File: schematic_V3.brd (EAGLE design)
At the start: 77.7 x 62.1 mm, 20 parts, among them IC1 VR1, J1 POWER_JACKPTH

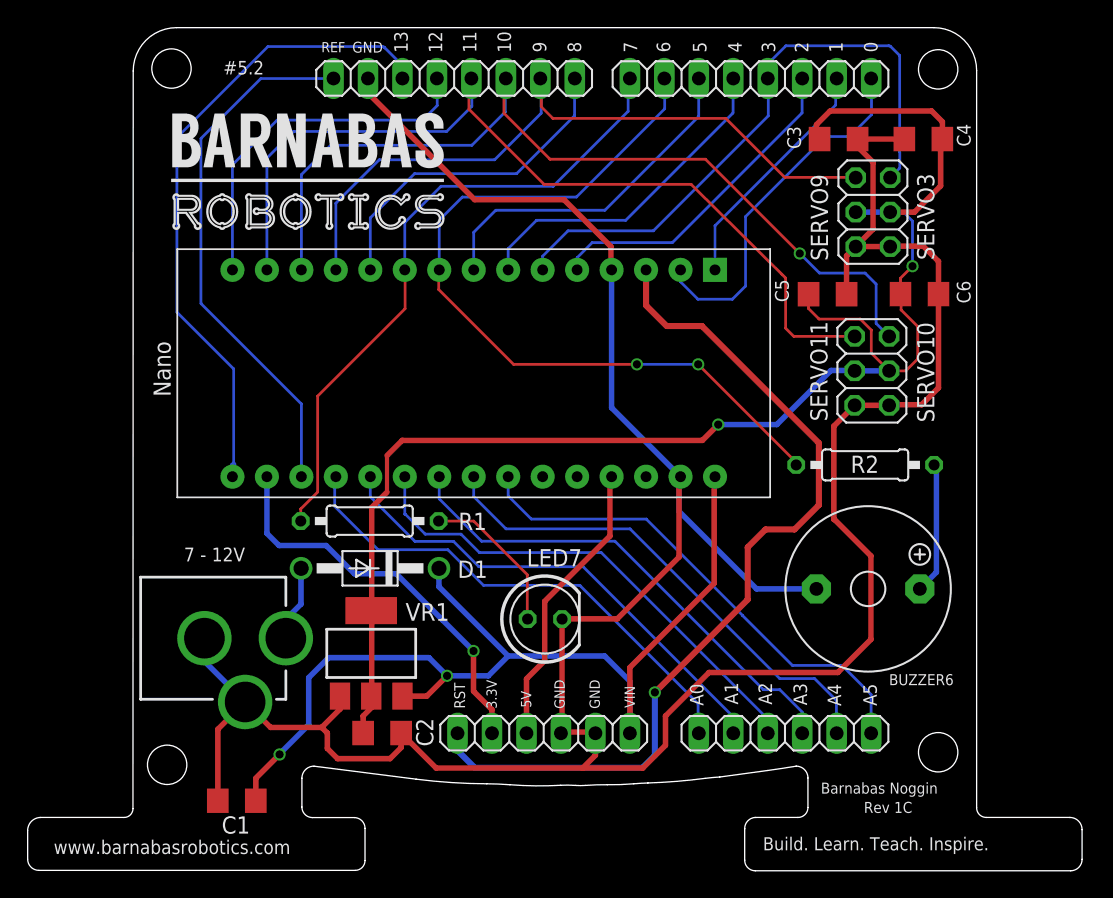
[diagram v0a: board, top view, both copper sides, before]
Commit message: Add files via upload
Connected 5VS and +5V rails. Minor cleanup of warnings prompted in Eagle
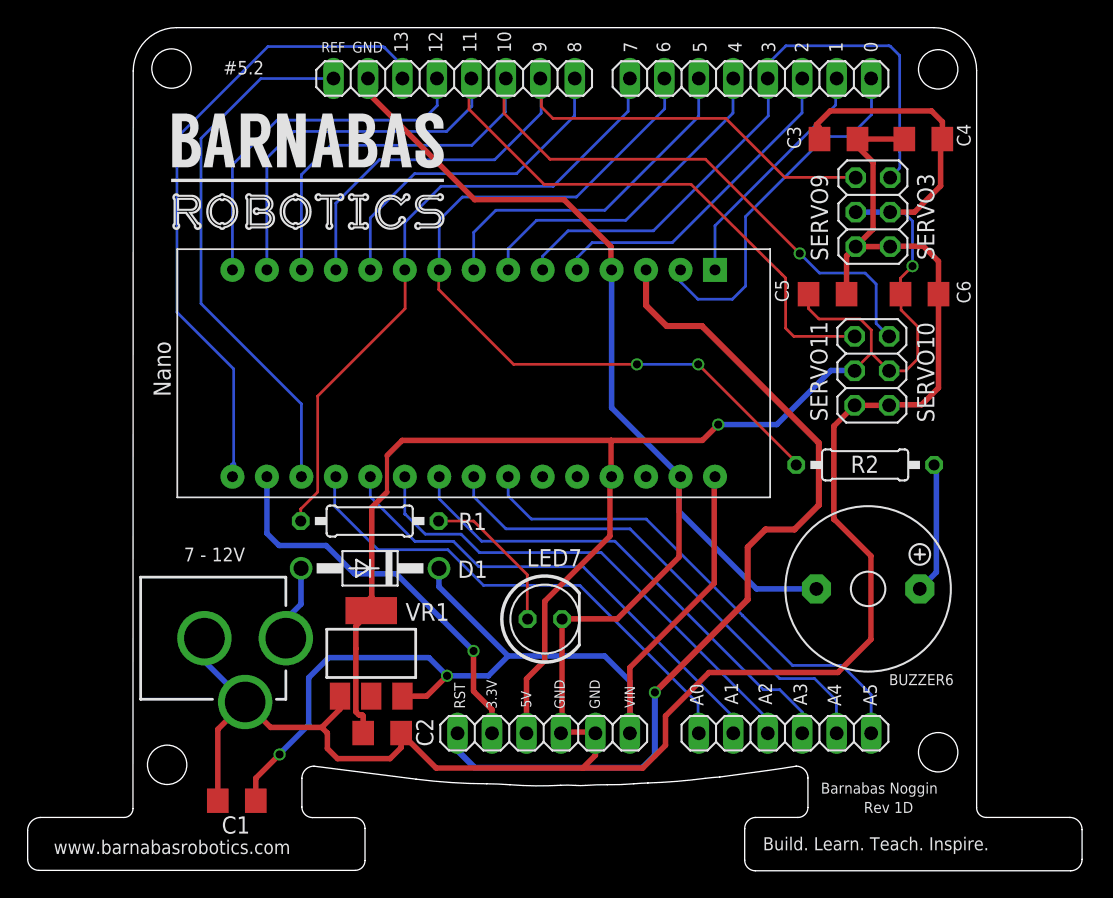
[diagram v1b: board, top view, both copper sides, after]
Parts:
- C1: value (none) -> 1μF
- C2: value (none) -> 10μF
- C3, C4, C5, C6: value (none) -> 0.1μF
- JP1, JP2, JP3, JP4, JP5, JP6: value (none) -> 2.54mm
- LED7: value (none) -> 5mm
- R1: value (none) -> 4.7K
- R2: value (none) -> 470
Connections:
- removed net 5VS: C2.1, C3.1, C4.1, C5.1, C6.1, IC1.4, JP5.3, JP5.4, JP6.3, JP6.4
- net +5V: now also C2.1, C3.1, C4.1, C5.1, C6.1, IC1.4, JP5.3, JP5.4, JP6.3, JP6.4
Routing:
- net +5V: track 21.5 -> 136.0 mm, vias 0 -> 2
- net 5VS: track 109.9 -> 0.00 mm, vias 2 -> 0
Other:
- board text added: "Rev 1D"
- board text removed: "Rev 1C"

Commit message: Thickened +5V traces
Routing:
- net +5V: track 136.0 -> 145.3 mm
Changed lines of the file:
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@@
 <wire x1="67.417" y1="53.825" x2="67.5416" y2="53.9496" width="0.4064" layer="1"/>
 <contactref element="C5" pad="1"/>
-<wire x1="57.6856" y1="42.5196" x2="57.6856" y2="41.4554" width="0.2032" layer="1"/>
-<wire x1="57.6856" y1="41.4554" x2="58.452" y2="40.689" width="0.2032" layer="1"/>
-<wire x1="58.452" y1="40.689" x2="61.494" y2="40.689" width="0.2032" layer="1"/>
-<wire x1="61.494" y1="40.689" x2="62.309" y2="39.874" width="0.2032" layer="1"/>
-<wire x1="62.309" y1="39.874" x2="62.309" y2="38.182928125" width="0.2032" layer="1"/>
+<wire x1="57.6856" y1="42.5196" x2="57.6856" y2="42.384" width="0.2032" layer="1"/>
 <contactref element="C6" pad="1"/>
-<wire x1="64.4604" y1="42.5244" x2="64.4604" y2="43.6984" width="0.2032" layer="1"/>
-<wire x1="64.4604" y1="43.6984" x2="65.345" y2="44.583" width="0.2032" layer="1"/>
 <via x="65.345" y="44.583" extent="1-16" drill="0.6"/>
-<wire x1="65.345" y1="44.583" x2="65.345" y2="47.903396875" width="0.2032" layer="16"/>
-<wire x1="65.733" y1="37.751" x2="64.852459375" y2="36.870459375" width="0.2032" layer="1"/>
-<wire x1="65.733" y1="37.751" x2="65.733" y2="40.126" width="0.2032" layer="1"/>
-<wire x1="65.733" y1="40.126" x2="64.502" y2="41.357" width="0.2032" layer="1"/>
-<wire x1="64.502" y1="41.357" x2="64.502" y2="42.4828" width="0.2032" layer="1"/>
-<wire x1="64.502" y1="42.4828" x2="64.4604" y2="42.5244" width="0.2032" layer="1"/>
+<wire x1="65.7235" y1="37.7415" x2="65.733" y2="37.751" width="0.2032" layer="1"/>
 <wire x1="65.345" y1="47.903396875" x2="64.7837" y2="48.464696875" width="0.2032" layer="16"/>
-<wire x1="64.7837" y1="48.464696875" x2="64.682" y2="48.566396875" width="0.2032" layer="16"/>
+<wire x1="64.682" y1="48.566396875" x2="64.7837" y2="48.464696875" width="0.2032" layer="16"/>
 <wire x1="24.861753125" y1="10.179265625" x2="24.861753125" y2="11.437753125" width="0.4064" layer="1"/>
 <wire x1="43.1704" y1="29.0712" x2="43.134" y2="29.1076" width="0.4064" layer="1"/>
 <wire x1="43.134" y1="29.1076" x2="43.134" y2="31.745" width="0.4064" layer="1"/>
-<wire x1="62.309" y1="38.182928125" x2="61.08146875" y2="36.955396875" width="0.2032" layer="1"/>
 <wire x1="61.08146875" y1="36.955396875" x2="61.08146875" y2="36.870459375" width="0.2032" layer="1"/>
-<wire x1="64.852459375" y1="36.870459375" x2="63.62146875" y2="36.870459375" width="0.2032" layer="1"/>
 <wire x1="65.487396875" y1="48.566396875" x2="63.69846875" y2="48.566396875" width="0.4064" layer="1"/>
 <wire x1="63.69846875" y1="48.566396875" x2="61.15846875" y2="48.566396875" width="0.4064" layer="16"/>
@@
 <wire x1="58.4932" y1="53.9496" x2="58.4932" y2="54.7898" width="0.4064" layer="1"/>
 <wire x1="58.4932" y1="54.7898" x2="58.27" y2="55.013" width="0.4064" layer="1"/>
-<wire x1="62.309" y1="38.182928125" x2="63.62146875" y2="36.870459375" width="0.2032" layer="1"/>
 <wire x1="64.7837" y1="48.464696875" x2="63.80016875" y2="48.464696875" width="0.2032" layer="16"/>
 <wire x1="63.80016875" y1="48.464696875" x2="63.69846875" y2="48.566396875" width="0.2032" layer="16"/>
@@
 <wire x1="24.861753125" y1="11.437753125" x2="24.779475" y2="11.52003125" width="0.4064" layer="1"/>
 <wire x1="24.779475" y1="11.52003125" x2="24.54993125" y2="11.52003125" width="0.4064" layer="1"/>
-<wire x1="24.32674375" y1="11.74321875" x2="24.32674375" y2="16.401" width="0.4064" layer="1"/>
-<wire x1="24.32674375" y1="16.401" x2="24.32674375" y2="18.06374375" width="0.4064" layer="1"/>
+<wire x1="24.32674375" y1="11.74321875" x2="24.32674375" y2="18.06374375" width="0.4064" layer="1"/>
 <wire x1="24.922" y1="18.659" x2="24.32674375" y2="18.06374375" width="0.4064" layer="1"/>
 <wire x1="25.495" y1="26.805" x2="25.495" y2="20.229" width="0.4064" layer="1"/>
@@
 <wire x1="25.45774375" y1="19.201028125" x2="24.922" y2="18.665284375" width="0.4064" layer="1"/>
 <wire x1="24.922" y1="18.665284375" x2="24.922" y2="18.659" width="0.4064" layer="1"/>
+<wire x1="61.08146875" y1="36.870459375" x2="62.335" y2="36.870459375" width="0.45" layer="1"/>
+<wire x1="62.335" y1="36.870459375" x2="63.62146875" y2="36.870459375" width="0.45" layer="1"/>
+<wire x1="63.62146875" y1="36.870459375" x2="64.852459375" y2="36.870459375" width="0.45" layer="1"/>
+<wire x1="64.852459375" y1="36.870459375" x2="65.7235" y2="37.7415" width="0.45" layer="1"/>
+<wire x1="65.733" y1="37.751" x2="65.733" y2="40.126" width="0.45" layer="1"/>
+<wire x1="65.733" y1="40.126" x2="64.4604" y2="41.3986" width="0.45" layer="1"/>
+<wire x1="64.4604" y1="41.3986" x2="64.4604" y2="42.5244" width="0.45" layer="1"/>
+<wire x1="64.4604" y1="42.5244" x2="64.4604" y2="43.6984" width="0.45" layer="1"/>
+<wire x1="64.4604" y1="43.6984" x2="65.345" y2="44.583" width="0.45" layer="1"/>
+<wire x1="65.345" y1="44.583" x2="65.345" y2="47.903396875" width="0.45" layer="16"/>
+<wire x1="65.345" y1="47.903396875" x2="64.682" y2="48.566396875" width="0.45" layer="16"/>
+<wire x1="63.69846875" y1="48.566396875" x2="64.682" y2="48.566396875" width="0.45" layer="16"/>
+<wire x1="61.15846875" y1="48.566396875" x2="58.81" y2="46.217928125" width="0.45" layer="1"/>
+<wire x1="58.81" y1="46.217928125" x2="58.81" y2="44.471" width="0.45" layer="1"/>
+<wire x1="58.81" y1="44.471" x2="57.6856" y2="43.3466" width="0.45" layer="1"/>
+<wire x1="57.6856" y1="43.3466" x2="57.6856" y2="42.384" width="0.45" layer="1"/>
+<wire x1="57.6856" y1="42.5196" x2="59.629934375" y2="40.575265625" width="0.45" layer="1"/>
+<wire x1="59.629934375" y1="40.575265625" x2="61.563946875" y2="40.575265625" width="0.45" layer="1"/>
+<wire x1="61.563946875" y1="40.575265625" x2="62.335" y2="39.8042125" width="0.45" layer="1"/>
+<wire x1="62.335" y1="39.8042125" x2="62.335" y2="36.870459375" width="0.45" layer="1"/>
 </signal>
 <signal name="3V3">
